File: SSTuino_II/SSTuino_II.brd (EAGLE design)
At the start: 68.6 x 25.4 mm, 90 parts, among them J1 TYPE-C-31-M-12, Q1 BSS138PS, Q2 BSS138PW, Q3 BSS138PS, Q4 BSS138PW, U1 MEGA4809, U2 ESP-32S, U3 ATSAMD11D14A-SSNT, U4 74HC4050, U5 74AHC1G125

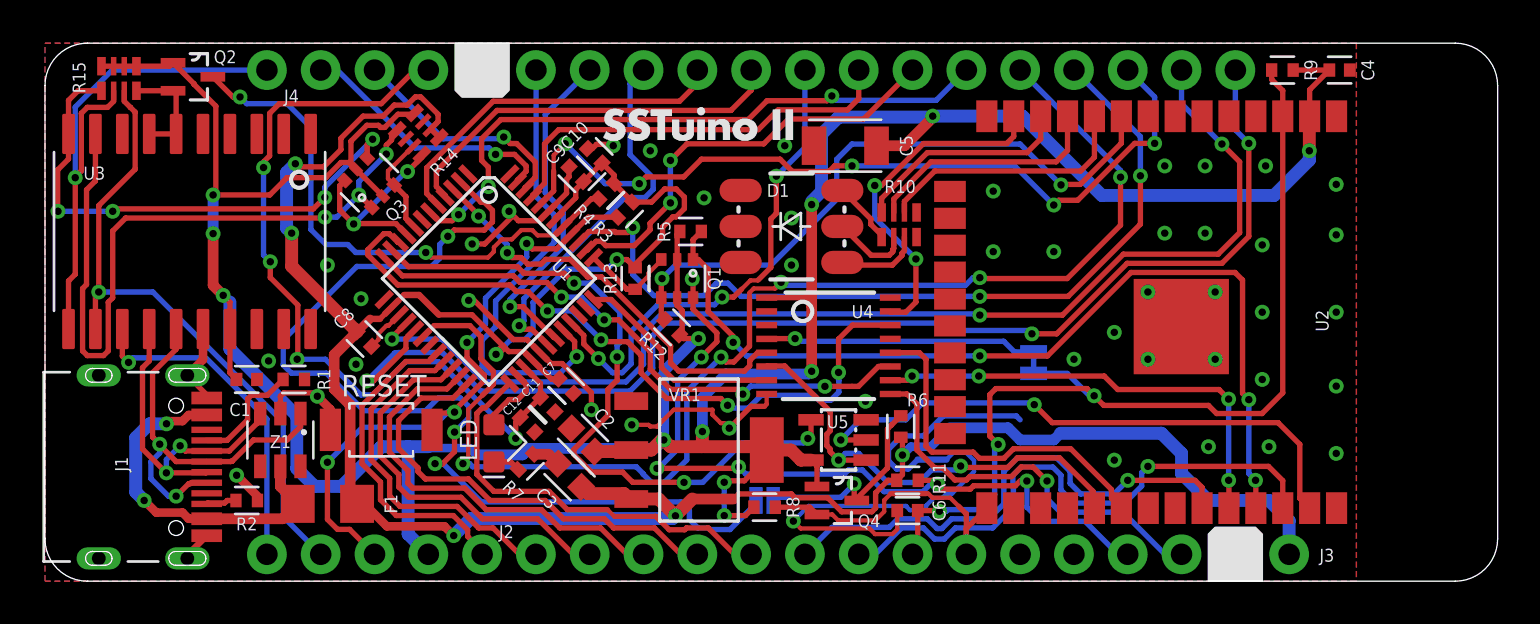
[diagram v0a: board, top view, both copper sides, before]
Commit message: added JST SH connector for SPI
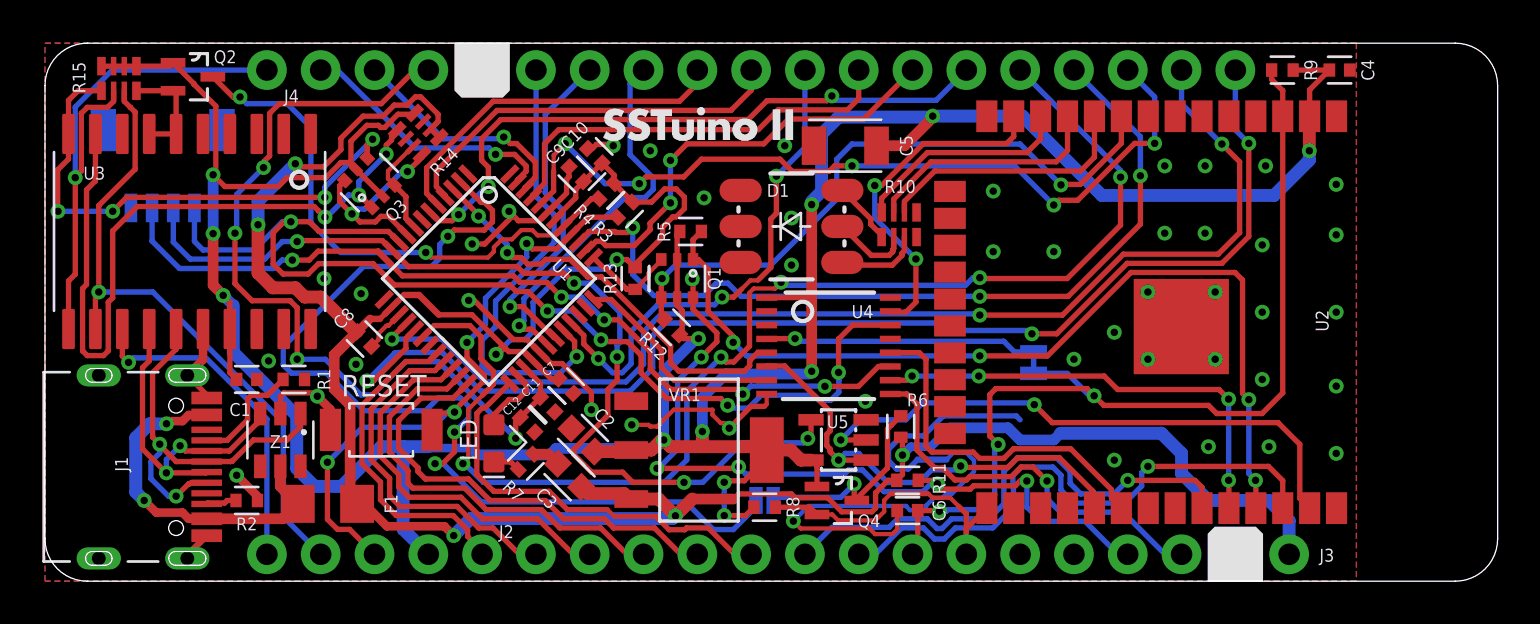
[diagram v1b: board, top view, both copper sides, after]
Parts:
- added SPI: (no value), SparkFun-Connectors:1X04_1MM_RA
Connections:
- net GND: now also SPI.1
- net PC0_MOSI: now also SPI.4
- net PC1_MISO: now also SPI.3
- net PC2_SCK: now also SPI.2
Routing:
- net PC0_MOSI: track 33.7 -> 51.1 mm, vias 4 -> 5
- net PC2_SCK: track 27.6 -> 41.1 mm, vias 4 -> 5
- net PC1_MISO: track 33.0 -> 45.8 mm, vias 4 -> 5
- net 5V: track 122.3 -> 124.6 mm
- net PD7_A7_AREF: track 38.0 -> 40.2 mm

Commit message: finalised SSTuino II main board
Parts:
- added J5: (no value), SparkFun-Connectors:1X01_NO_SILK
- J3: device SparkFun-Connectors:1X06_NO_SILK -> SparkFun-Connectors:1X19_NO_SILK
- J4: device SparkFun-Connectors:1X19_NO_SILK -> SparkFun-Connectors:1X06_NO_SILK
- moved J3 25.0 mm to (56.2, 24.1), turned to 180 degrees
- moved J4 25.0 mm to (46.0, 1.27), turned to 0 degrees
- moved R9 3.49 mm to (61.9, 24.1), turned to 90 degrees
- moved C4 0.48 mm to (60.6, 24.1), turned to 270 degrees
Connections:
- net 5V: now also J4.6; no longer J3.6
- net ESP_RX_5V: now also J4.4; no longer J3.4
- net ESP_TX_5V: now also J4.3; no longer J3.3
- net GND: now also J3.15, J4.5; no longer J3.5, J4.15
- net PA0_D2: now also J3.3; no longer J4.3
- net PA1_D7: now also J3.8; no longer J4.8
- net PA2_D20_SDA: now also J3.17; no longer J4.17
- net PA3_D21_SCL: now also J3.18; no longer J4.18
- net PB0_D9~: now also J3.10; no longer J4.10
- net PB1_D10~: now also J3.11; no longer J4.11
- net PB2_D5~: now also J3.6; no longer J4.6
- net PC4_D1_TX1: now also J3.2; no longer J4.2
- net PC5_D0_RX1: now also J3.1; no longer J4.1
- net PC6_D4: now also J3.5; no longer J4.5
- net PD7_A7_AREF: now also J3.16; no longer J4.16
- net PE0_D11: now also J3.12; no longer J4.12
- net PE1_D12: now also J3.13; no longer J4.13
- net PE2_D13: now also J3.14; no longer J4.14
- net PE3_D8: now also J3.9; no longer J4.9
- net PF4_D6~: now also J3.7; no longer J4.7
- net PF5_D3~: now also J3.4; no longer J4.4
- net RESETN: now also J3.19; no longer J4.19
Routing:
- net ESP_EN: track 44.7 -> 52.4 mm
- net GND: track 69.0 -> 70.8 mm
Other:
- board text added: "MOSI MISO SCK GND"
